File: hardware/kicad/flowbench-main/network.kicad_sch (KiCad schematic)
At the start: 23 parts, among them J6 WIZ850io J1, J7 WIZ850io J2, J8 microSD push-push

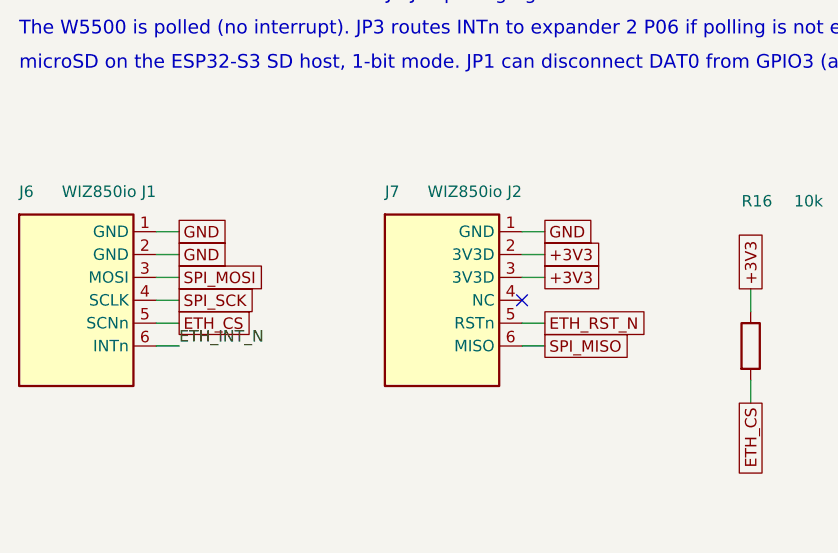
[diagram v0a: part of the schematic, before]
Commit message: KiCad: fix off-grid pins on ADS1219 and AM26C31 symbols
A floating-point modulo misread the symbol half-height as off-grid and
shifted it by half a step, leaving top and bottom pins 0.635 mm off the
1.27 mm connection grid (16 ERC warnings). verify.py now checks every pin
and wire end against the grid.

Co-Authored-By: Claude Opus 5.5 <noreply@anthropic.com>
Claude-Session: https://claude.ai/code/session_01QEmmugJA9S77dSDSNcKrPa
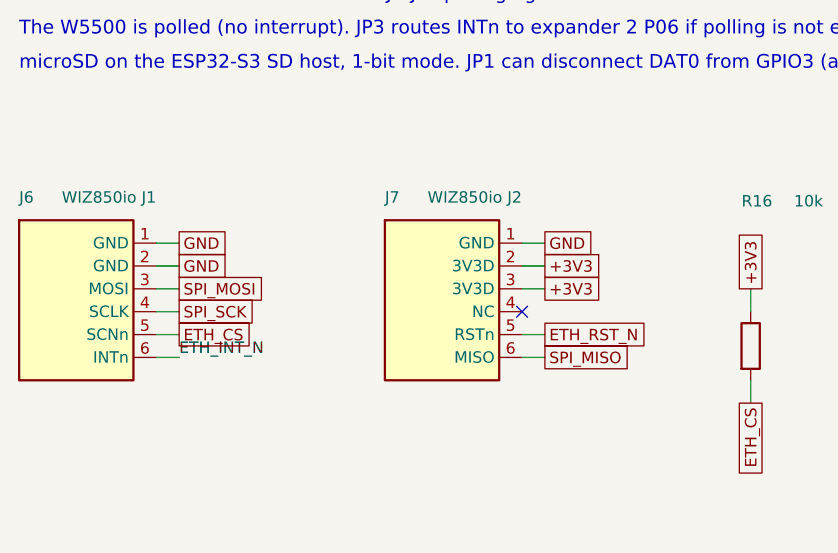
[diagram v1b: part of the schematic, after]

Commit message: KiCad: WIZ850io as one part with a two-row footprint
Pinout and size confirmed from the module (20 x 25 mm, two 1x6 headers).
The two header symbols become one 12-pin WIZ850io part on footprint
FlowBench:WIZ850io (J1 pads 1-6, J2 pads 7-12, rows 17.78 mm apart), so the
headers can't be placed at the wrong spacing.

Co-Authored-By: Claude Opus 5.5 <noreply@anthropic.com>
Claude-Session: https://claude.ai/code/session_01QEmmugJA9S77dSDSNcKrPa
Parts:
- removed J6: WIZ850io J1, Connector_PinSocket_2.54mm:PinSocket_1x06_P2.54mm_Vertical, symbol FlowBench:WIZ850io_J1
- removed J7: WIZ850io J2, Connector_PinSocket_2.54mm:PinSocket_1x06_P2.54mm_Vertical, symbol FlowBench:WIZ850io_J2
- removed J8: microSD push-push, Connector_Card:microSD_HC_Hirose_DM3AT-SF-PEJM5, symbol FlowBench:Micro_SD_Card_Det
- added J6: microSD push-push, Connector_Card:microSD_HC_Hirose_DM3AT-SF-PEJM5, symbol FlowBench:Micro_SD_Card_Det
- added U2: WIZ850io, FlowBench:WIZ850io, symbol FlowBench:WIZ850io
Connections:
- net +3V3: now also J6.4 (VDD), U2.8 (J2-2 3V3D), U2.9 (J2-3 3V3D)
- net ETH_CS: now also U2.5 (J1-5 SCNn)
- net ETH_INT_N: now also U2.6 (J1-6 INTn)
- net ETH_RST_N: now also U2.11 (J2-5 RSTn)
- net GND: now also J6.11 (SHIELD), J6.6 (VSS), J6.9 (DET_B), U2.1 (J1-1 GND), U2.2 (J1-2 GND), U2.7 (J2-1 GND)
- net SD_CD_N: now also J6.10 (DET_A)
- net SD_CLK: now also J6.5 (CLK)
- net SD_CMD: now also J6.3 (CMD)
- net SD_DAT0: now also J6.7 (DAT0)
- net SD_DAT1: now also J6.8 (DAT1)
- net SD_DAT2: now also J6.1 (DAT2)
- net SD_DAT3: now also J6.2 (DAT3/CD)
- net SPI_MISO: now also U2.12 (J2-6 MISO)
- net SPI_MOSI: now also U2.3 (J1-3 MOSI)
- net SPI_SCK: now also U2.4 (J1-4 SCLK)
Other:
- note added: "WIZ850io: one footprint with both 1x6 sockets (J1 = pads 1-6, J2 = pads 7-12), rows 17.78 mm (0.7 in) apart."
- note removed: "WIZ850io: two 1x6 sockets. Check the J1-J2 spacing against the WIZnet mechanical drawing before layout."

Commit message: KiCad: DevKit as one part with a 25.4 mm two-row footprint
Header pinout confirmed against Espressif's J1/J3 tables; row spacing measured
at 25.4 mm. The two header symbols become one 44-pin ESP32-S3-DevKitC-1 part on
footprint FlowBench:ESP32-S3-DevKitC-1 (J1 pads 1-22, J3 pads 23-44), with the
antenna end marked. BOM notes the N32R16V as a drop-in alternative.

Co-Authored-By: Claude Opus 5.5 <noreply@anthropic.com>
Claude-Session: https://claude.ai/code/session_01QEmmugJA9S77dSDSNcKrPa
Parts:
- removed J6: microSD push-push, Connector_Card:microSD_HC_Hirose_DM3AT-SF-PEJM5, symbol FlowBench:Micro_SD_Card_Det
- removed U2: WIZ850io, FlowBench:WIZ850io, symbol FlowBench:WIZ850io
- added J4: microSD push-push, Connector_Card:microSD_HC_Hirose_DM3AT-SF-PEJM5, symbol FlowBench:Micro_SD_Card_Det
- added U3: WIZ850io, FlowBench:WIZ850io, symbol FlowBench:WIZ850io
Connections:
- net +3V3: now also J4.4 (VDD), U3.8 (J2-2 3V3D), U3.9 (J2-3 3V3D)
- net ETH_CS: now also U3.5 (J1-5 SCNn)
- net ETH_INT_N: now also U3.6 (J1-6 INTn)
- net ETH_RST_N: now also U3.11 (J2-5 RSTn)
- net GND: now also J4.11 (SHIELD), J4.6 (VSS), J4.9 (DET_B), U3.1 (J1-1 GND), U3.2 (J1-2 GND), U3.7 (J2-1 GND)
- net SD_CD_N: now also J4.10 (DET_A)
- net SD_CLK: now also J4.5 (CLK)
- net SD_CMD: now also J4.3 (CMD)
- net SD_DAT0: now also J4.7 (DAT0)
- net SD_DAT1: now also J4.8 (DAT1)
- net SD_DAT2: now also J4.1 (DAT2)
- net SD_DAT3: now also J4.2 (DAT3/CD)
- net SPI_MISO: now also U3.12 (J2-6 MISO)
- net SPI_MOSI: now also U3.3 (J1-3 MOSI)
- net SPI_SCK: now also U3.4 (J1-4 SCLK)

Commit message: KiCad: microSD shield pin numbered SH to match the Hirose footprint
Update PCB from Schematic reported "pad SH not in symbol" and "pad 11 not
found": the DM3AT footprint names its shield pads SH. The symbol's shield pin
is renumbered SH (still on GND).

Co-Authored-By: Claude Opus 5.5 <noreply@anthropic.com>
Claude-Session: https://claude.ai/code/session_01QEmmugJA9S77dSDSNcKrPa
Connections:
- net GND: now also J4.SH (SHIELD); no longer J4.11 (SHIELD)
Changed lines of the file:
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@@
   (pin "11")
   (pin "12")
-  (instances (project "flowbench-main" (path "/4045a581-0549-438d-8242-1a9451537e5e/3ea2a2ee-6bae-405b-a3f0-a56d414c8ef0" (reference "U3") (unit 1))))
+  (instances (project "flowbench-main" (path "/502a429a-bd12-4b4a-9a13-ff490f4e7ad9/9a464bbf-ae22-4e47-909e-46313454a25a" (reference "U3") (unit 1))))
 )
 (wire (pts (xy 35.56 46.99) (xy 33.02 46.99)) (stroke (width 0) (type default)))
@@
   (pin "1")
   (pin "2")
-  (instances (project "flowbench-main" (path "/4045a581-0549-438d-8242-1a9451537e5e/3ea2a2ee-6bae-405b-a3f0-a56d414c8ef0" (reference "R16") (unit 1))))
+  (instances (project "flowbench-main" (path "/502a429a-bd12-4b4a-9a13-ff490f4e7ad9/9a464bbf-ae22-4e47-909e-46313454a25a" (reference "R16") (unit 1))))
 )
 (wire (pts (xy 88.9 54.61) (xy 88.9 52.07)) (stroke (width 0) (type default)))
@@
   (pin "1")
   (pin "2")
-  (instances (project "flowbench-main" (path "/4045a581-0549-438d-8242-1a9451537e5e/3ea2a2ee-6bae-405b-a3f0-a56d414c8ef0" (reference "R17") (unit 1))))
+  (instances (project "flowbench-main" (path "/502a429a-bd12-4b4a-9a13-ff490f4e7ad9/9a464bbf-ae22-4e47-909e-46313454a25a" (reference "R17") (unit 1))))
 )
 (wire (pts (xy 101.6 54.61) (xy 101.6 52.07)) (stroke (width 0) (type default)))
@@
   (pin "1")
   (pin "2")
-  (instances (project "flowbench-main" (path "/4045a581-0549-438d-8242-1a9451537e5e/3ea2a2ee-6bae-405b-a3f0-a56d414c8ef0" (reference "R18") (unit 1))))
+  (instances (project "flowbench-main" (path "/502a429a-bd12-4b4a-9a13-ff490f4e7ad9/9a464bbf-ae22-4e47-909e-46313454a25a" (reference "R18") (unit 1))))
 )
 (wire (pts (xy 114.3 54.61) (xy 114.3 52.07)) (stroke (width 0) (type default)))
@@
   (pin "1")
   (pin "2")
-  (instances (project "flowbench-main" (path "/4045a581-0549-438d-8242-1a9451537e5e/3ea2a2ee-6bae-405b-a3f0-a56d414c8ef0" (reference "JP1") (unit 1))))
+  (instances (project "flowbench-main" (path "/502a429a-bd12-4b4a-9a13-ff490f4e7ad9/9a464bbf-ae22-4e47-909e-46313454a25a" (reference "JP1") (unit 1))))
 )
 (wire (pts (xy 139.7 45.72) (xy 137.16 45.72)) (stroke (width 0) (type default)))
@@
   (pin "1")
   (pin "2")
-  (instances (project "flowbench-main" (path "/4045a581-0549-438d-8242-1a9451537e5e/3ea2a2ee-6bae-405b-a3f0-a56d414c8ef0" (reference "C6") (unit 1))))
+  (instances (project "flowbench-main" (path "/502a429a-bd12-4b4a-9a13-ff490f4e7ad9/9a464bbf-ae22-4e47-909e-46313454a25a" (reference "C6") (unit 1))))
 )
 (wire (pts (xy 176.53 54.61) (xy 176.53 52.07)) (stroke (width 0) (type default)))
@@
   (pin "1")
   (pin "2")
-  (instances (project "flowbench-main" (path "/4045a581-0549-438d-8242-1a9451537e5e/3ea2a2ee-6bae-405b-a3f0-a56d414c8ef0" (reference "C7") (unit 1))))
+  (instances (project "flowbench-main" (path "/502a429a-bd12-4b4a-9a13-ff490f4e7ad9/9a464bbf-ae22-4e47-909e-46313454a25a" (reference "C7") (unit 1))))
 )
 (wire (pts (xy 190.5 54.61) (xy 190.5 52.07)) (stroke (width 0) (type default)))
@@
   (pin "1")
   (pin "10")
-  (pin "11")
+  (pin "SH")
   (pin "2")
   (pin "3")
@@
   (pin "8")
   (pin "9")
-  (instances (project "flowbench-main" (path "/4045a581-0549-438d-8242-1a9451537e5e/3ea2a2ee-6bae-405b-a3f0-a56d414c8ef0" (reference "J4") (unit 1))))
+  (instances (project "flowbench-main" (path "/502a429a-bd12-4b4a-9a13-ff490f4e7ad9/9a464bbf-ae22-4e47-909e-46313454a25a" (reference "J4") (unit 1))))
 )
 (wire (pts (xy 215.9 50.8) (xy 213.36 50.8)) (stroke (width 0) (type default)))
@@
   (pin "1")
   (pin "2")
-  (instances (project "flowbench-main" (path "/4045a581-0549-438d-8242-1a9451537e5e/3ea2a2ee-6bae-405b-a3f0-a56d414c8ef0" (reference "R19") (unit 1))))
+  (instances (project "flowbench-main" (path "/502a429a-bd12-4b4a-9a13-ff490f4e7ad9/9a464bbf-ae22-4e47-909e-46313454a25a" (reference "R19") (unit 1))))
 )
 (wire (pts (xy 279.4 54.61) (xy 279.4 52.07)) (stroke (width 0) (type default)))
@@
   (pin "1")
   (pin "2")
-  (instances (project "flowbench-main" (path "/4045a581-0549-438d-8242-1a9451537e5e/3ea2a2ee-6bae-405b-a3f0-a56d414c8ef0" (reference "R20") (unit 1))))
+  (instances (project "flowbench-main" (path "/502a429a-bd12-4b4a-9a13-ff490f4e7ad9/9a464bbf-ae22-4e47-909e-46313454a25a" (reference "R20") (unit 1))))
 )
 (wire (pts (xy 290.83 54.61) (xy 290.83 52.07)) (stroke (width 0) (type default)))
@@
   (pin "1")
   (pin "2")
-  (instances (project "flowbench-main" (path "/4045a581-0549-438d-8242-1a9451537e5e/3ea2a2ee-6bae-405b-a3f0-a56d414c8ef0" (reference "R21") (unit 1))))
+  (instances (project "flowbench-main" (path "/502a429a-bd12-4b4a-9a13-ff490f4e7ad9/9a464bbf-ae22-4e47-909e-46313454a25a" (reference "R21") (unit 1))))
 )
 (wire (pts (xy 303.53 54.61) (xy 303.53 52.07)) (stroke (width 0) (type default)))
@@
   (pin "1")
   (pin "2")
-  (instances (project "flowbench-main" (path "/4045a581-0549-438d-8242-1a9451537e5e/3ea2a2ee-6bae-405b-a3f0-a56d414c8ef0" (reference "R22") (unit 1))))
+  (instances (project "flowbench-main" (path "/502a429a-bd12-4b4a-9a13-ff490f4e7ad9/9a464bbf-ae22-4e47-909e-46313454a25a" (reference "R22") (unit 1))))
 )
 (wire (pts (xy 316.23 54.61) (xy 316.23 52.07)) (stroke (width 0) (type default)))
@@
   (pin "1")
   (pin "2")
-  (instances (project "flowbench-main" (path "/4045a581-0549-438d-8242-1a9451537e5e/3ea2a2ee-6bae-405b-a3f0-a56d414c8ef0" (reference "R23") (unit 1))))
+  (instances (project "flowbench-main" (path "/502a429a-bd12-4b4a-9a13-ff490f4e7ad9/9a464bbf-ae22-4e47-909e-46313454a25a" (reference "R23") (unit 1))))
 )
 (wire (pts (xy 327.66 54.61) (xy 327.66 52.07)) (stroke (width 0) (type default)))
@@
   (pin "1")
   (pin "2")
-  (instances (project "flowbench-main" (path "/4045a581-0549-438d-8242-1a9451537e5e/3ea2a2ee-6bae-405b-a3f0-a56d414c8ef0" (reference "R24") (unit 1))))
+  (instances (project "flowbench-main" (path "/502a429a-bd12-4b4a-9a13-ff490f4e7ad9/9a464bbf-ae22-4e47-909e-46313454a25a" (reference "R24") (unit 1))))
 )
 (wire (pts (xy 340.36 54.61) (xy 340.36 52.07)) (stroke (width 0) (type default)))
@@
   (pin "1")
   (pin "2")
-  (instances (project "flowbench-main" (path "/4045a581-0549-438d-8242-1a9451537e5e/3ea2a2ee-6bae-405b-a3f0-a56d414c8ef0" (reference "R25") (unit 1))))
+  (instances (project "flowbench-main" (path "/502a429a-bd12-4b4a-9a13-ff490f4e7ad9/9a464bbf-ae22-4e47-909e-46313454a25a" (reference "R25") (unit 1))))
 )
 (wire (pts (xy 351.79 60.96) (xy 351.79 58.42)) (stroke (width 0) (type default)))
@@
   (pin "1")
   (pin "2")
-  (instances (project "flowbench-main" (path "/4045a581-0549-438d-8242-1a9451537e5e/3ea2a2ee-6bae-405b-a3f0-a56d414c8ef0" (reference "JP2") (unit 1))))
+  (instances (project "flowbench-main" (path "/502a429a-bd12-4b4a-9a13-ff490f4e7ad9/9a464bbf-ae22-4e47-909e-46313454a25a" (reference "JP2") (unit 1))))
 )
 (wire (pts (xy 381 45.72) (xy 378.46 45.72)) (stroke (width 0) (type default)))
@@
   (pin "1")
   (pin "2")
-  (instances (project "flowbench-main" (path "/4045a581-0549-438d-8242-1a9451537e5e/3ea2a2ee-6bae-405b-a3f0-a56d414c8ef0" (reference "C8") (unit 1))))
+  (instances (project "flowbench-main" (path "/502a429a-bd12-4b4a-9a13-ff490f4e7ad9/9a464bbf-ae22-4e47-909e-46313454a25a" (reference "C8") (unit 1))))
 )
 (wire (pts (xy 412.75 54.61) (xy 412.75 52.07)) (stroke (width 0) (type default)))
@@
   (pin "1")
   (pin "2")
-  (instances (project "flowbench-main" (path "/4045a581-0549-438d-8242-1a9451537e5e/3ea2a2ee-6bae-405b-a3f0-a56d414c8ef0" (reference "C9") (unit 1))))
+  (instances (project "flowbench-main" (path "/502a429a-bd12-4b4a-9a13-ff490f4e7ad9/9a464bbf-ae22-4e47-909e-46313454a25a" (reference "C9") (unit 1))))
 )
 (wire (pts (xy 427.99 54.61) (xy 427.99 52.07)) (stroke (width 0) (type default)))
@@
   (property "Datasheet" "~" (at 440.69 48.26 0) (effects (font (size 1.27 1.27)) (justify left) hide))
   (pin "1")
-  (instances (project "flowbench-main" (path "/4045a581-0549-438d-8242-1a9451537e5e/3ea2a2ee-6bae-405b-a3f0-a56d414c8ef0" (reference "TP13") (unit 1))))
+  (instances (project "flowbench-main" (path "/502a429a-bd12-4b4a-9a13-ff490f4e7ad9/9a464bbf-ae22-4e47-909e-46313454a25a" (reference "TP13") (unit 1))))
 )
 (wire (pts (xy 440.69 48.26) (xy 440.69 50.8)) (stroke (width 0) (type default)))
@@
   (property "Datasheet" "~" (at 452.12 48.26 0) (effects (font (size 1.27 1.27)) (justify left) hide))
   (pin "1")
-  (instances (project "flowbench-main" (path "/4045a581-0549-438d-8242-1a9451537e5e/3ea2a2ee-6bae-405b-a3f0-a56d414c8ef0" (reference "TP14") (unit 1))))
+  (instances (project "flowbench-main" (path "/502a429a-bd12-4b4a-9a13-ff490f4e7ad9/9a464bbf-ae22-4e47-909e-46313454a25a" (reference "TP14") (unit 1))))
 )
 (wire (pts (xy 452.12 48.26) (xy 452.12 50.8)) (stroke (width 0) (type default)))
@@
   (property "Datasheet" "~" (at 463.55 48.26 0) (effects (font (size 1.27 1.27)) (justify left) hide))
   (pin "1")
-  (instances (project "flowbench-main" (path "/4045a581-0549-438d-8242-1a9451537e5e/3ea2a2ee-6bae-405b-a3f0-a56d414c8ef0" (reference "TP15") (unit 1))))
+  (instances (project "flowbench-main" (path "/502a429a-bd12-4b4a-9a13-ff490f4e7ad9/9a464bbf-ae22-4e47-909e-46313454a25a" (reference "TP15") (unit 1))))
 )
 (wire (pts (xy 463.55 48.26) (xy 463.55 50.8)) (stroke (width 0) (type default)))
@@
   (property "Datasheet" "~" (at 474.98 48.26 0) (effects (font (size 1.27 1.27)) (justify left) hide))
   (pin "1")
-  (instances (project "flowbench-main" (path "/4045a581-0549-438d-8242-1a9451537e5e/3ea2a2ee-6bae-405b-a3f0-a56d414c8ef0" (reference "TP16") (unit 1))))
+  (instances (project "flowbench-main" (path "/502a429a-bd12-4b4a-9a13-ff490f4e7ad9/9a464bbf-ae22-4e47-909e-46313454a25a" (reference "TP16") (unit 1))))
 )
 (wire (pts (xy 474.98 48.26) (xy 474.98 50.8)) (stroke (width 0) (type default)))
